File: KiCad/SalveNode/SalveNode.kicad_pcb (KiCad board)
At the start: 2 copper layers, 42.8 x 31 mm, 22 parts, among them IC1 DS89C21TMX_NOPB, IC2 TMP75AQDGKRQ1, IC3 VEML7700-TR, J1 AVR-ISP-6, J3 691382030006, U1 MCP1700x-330xxTT, U2 ATmega328PB-A, Y1 16M

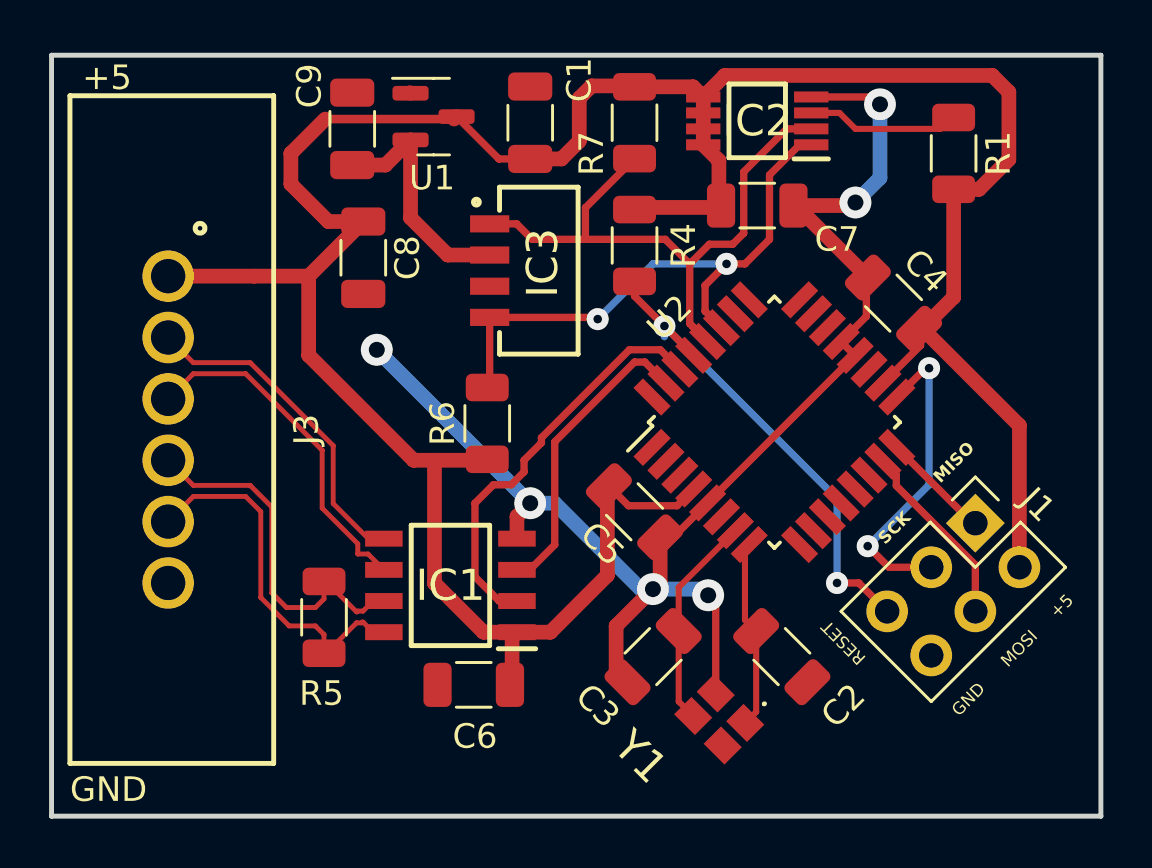
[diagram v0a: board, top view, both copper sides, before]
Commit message: modified schematics and continued development of Arduino programs
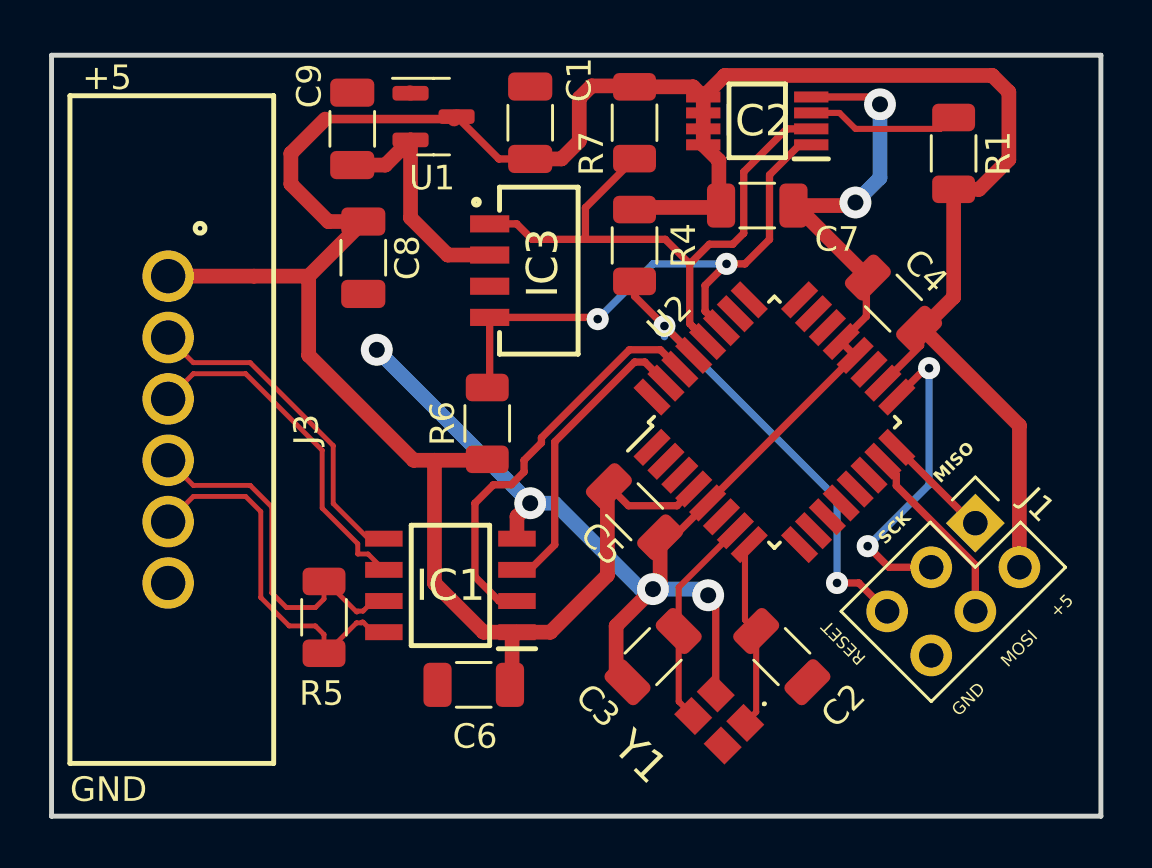
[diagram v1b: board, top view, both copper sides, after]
